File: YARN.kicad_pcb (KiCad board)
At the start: 2 copper layers, 99 x 91.7 mm, 12 parts, among them J1 Cart System Out, J2 Cart Main In, J3 Cart Sub In, SW1 SW_SPDT, U1 74HC244, U2 74HC244

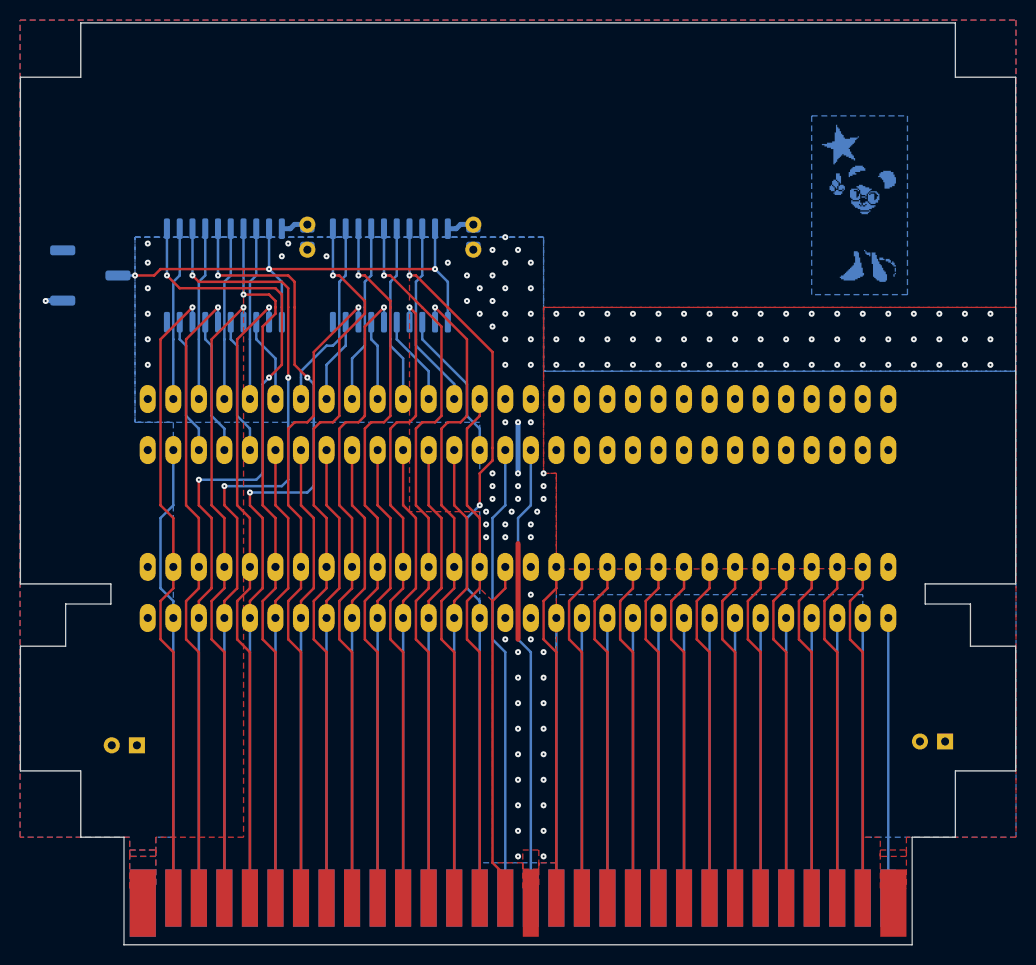
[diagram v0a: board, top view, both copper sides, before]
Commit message: Buffer data and addr bus, add switch for VRC6 A/B
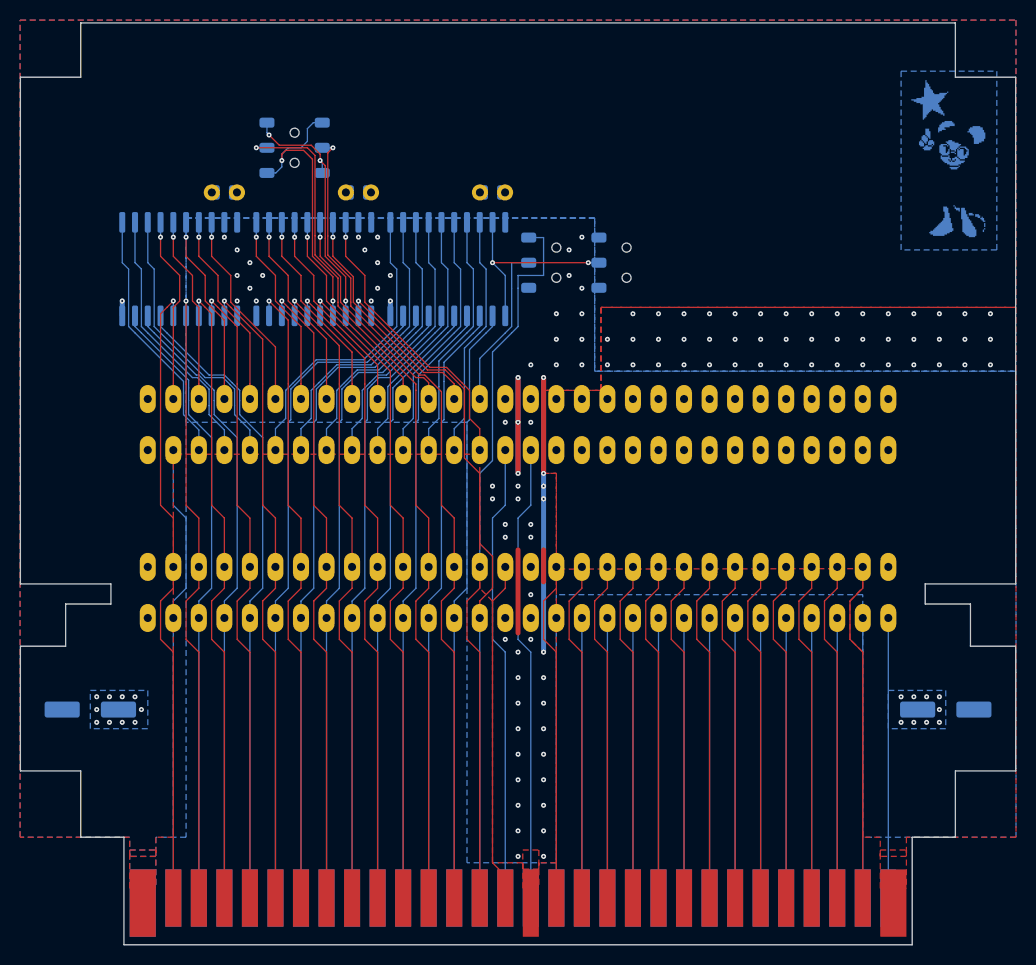
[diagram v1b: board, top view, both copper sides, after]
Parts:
- removed the C4 at (106.0, 67.3)
- added C2: 0.1uF, YARN:C_Disc-0805_D3.0mm_W1.6mm_P2.50mm, B.Cu at (111.1, 62.9)
- added C3: 0.1uF, YARN:C_Disc-0805_D3.0mm_W1.6mm_P2.50mm, B.Cu at (97.8, 62.9)
- added SW2: SW_SPDT, YARN:SK-3390A-L0, B.Cu at (130.8, 69.8)
- added SW3: SW_DPDT_x2, YARN:SS-3390S-L0, B.Cu at (104.8, 58.4)
- added U3: 74HC541, Package_SO:SOIC-20W_7.5x12.8mm_P1.27mm, B.Cu at (93.3, 70.5)
- C4: renamed from C2; footprint Capacitor_THT:CP_Radial_D5.0mm_P2.50mm -> Capacitor_SMD:CP_Elec_6.3x5.4
- C5: renamed from C3; footprint Capacitor_THT:CP_Radial_D5.0mm_P2.50mm -> Capacitor_SMD:CP_Elec_6.3x5.4
- J3: value Cart Sub In -> Cart Exp In
- LOGO-2: renamed from Ref**; value Val** -> YARN
- SW1: footprint YARN:JS102011SCQN -> YARN:SK-3390A-L0
- U1, U2: value 74HC244 -> 74HC541
- moved SW1 53.4 mm to (137.8, 69.8), turned to -90 degrees
- moved LOGO-2 11.4 mm to (149.9, 57.8)
- moved LOGO-1 9.94 mm to (169.5, 59.7)
- moved U2 8.91 mm to (106.7, 70.5)
- moved C5 5.84 mm to (84.5, 114.3), turned to 0 degrees
- moved U1 5.75 mm to (120.0, 70.5)
- moved C1 4.84 mm to (124.5, 62.9), turned to 180 degrees
- moved C4 3.18 mm to (169.5, 114.3), turned to 0 degrees
- renumbered REF** to LOGO-1
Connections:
- J3 pad 14: /CPU_R~{W} -> /S_CPU_R~{W}
- J3 pad 36: /CPU_D7 -> /S_CPU_D7
- J3 pad 37: /CPU_D6 -> /S_CPU_D6
- J3 pad 38: /CPU_D5 -> /S_CPU_D5
- J3 pad 39: /CPU_D4 -> /S_CPU_D4
- J3 pad 40: /CPU_D3 -> /S_CPU_D3
- J3 pad 41: /CPU_D2 -> /S_CPU_D2
- J3 pad 42: /CPU_D1 -> /S_CPU_D1
- J3 pad 43: /CPU_D0 -> /S_CPU_D0
- U1 pad 11: /CPU_A5 -> /S_CPU_D7
- U1 pad 12: /S_CPU_A6 -> /S_CPU_D6
- U1 pad 13: /CPU_A3 -> /S_CPU_D5
- U1 pad 14: /S_CPU_A4 -> /S_CPU_D4
- U1 pad 15: /CPU_A1 -> /S_CPU_D3
- U1 pad 16: /S_CPU_A2 -> /S_CPU_D2
- U1 pad 17: /~{ROMSEL} -> /S_CPU_D1
- U1 pad 18: /S_CPU_A0 -> /S_CPU_D0
- U1 pad 2: /CPU_A0 -> /CPU_D0
- U1 pad 3: /S_~{ROMSEL} -> /CPU_D1
- U1 pad 4: /CPU_A2 -> /CPU_D2
- U1 pad 5: /S_CPU_A1 -> /CPU_D3
- U1 pad 6: /CPU_A4 -> /CPU_D4
- U1 pad 7: /S_CPU_A3 -> /CPU_D5
- U1 pad 8: /CPU_A6 -> /CPU_D6
- U1 pad 9: /S_CPU_A5 -> /CPU_D7
- U2 pad 1: /S_~{CE} -> GND
- U2 pad 11: /CPU_A12 -> /S_CPU_A6
- U2 pad 12: /S_CPU_A11 -> /S_CPU_A5
- U2 pad 13: /CPU_A13 -> /S_CPU_A4
- U2 pad 14: /S_CPU_A10 -> /S_CPU_A3
- U2 pad 15: /CPU_A14 -> /S_CPU_A2
- U2 pad 16: /S_CPU_A9 -> /S_CPU_A1
- U2 pad 17: /CPU_A7 -> /S_CPU_A0
- U2 pad 18: /S_CPU_A8 -> /S_~{ROMSEL}
- U2 pad 19: /S_~{CE} -> GND
- U2 pad 2: /CPU_A8 -> /~{ROMSEL}
- U2 pad 3: /S_CPU_A7 -> /CPU_A0_V
- U2 pad 4: /CPU_A9 -> /CPU_A1_V
- U2 pad 5: /S_CPU_A14 -> /CPU_A2
- U2 pad 6: /CPU_A10 -> /CPU_A3
- U2 pad 7: /S_CPU_A13 -> /CPU_A4
- U2 pad 8: /CPU_A11 -> /CPU_A5
- U2 pad 9: /S_CPU_A12 -> /CPU_A6
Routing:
- net GND: track 16.3 -> 70.3 mm, vias 73 -> 76
- net /S_~{CE}: track 51.5 -> 20.4 mm, vias 3 -> 2
- net /S_CPU_D7: track 0.00 -> 30.7 mm
- net /CPU_A1_V: track 0.00 -> 29.7 mm, vias 0 -> 2
- net /S_CPU_D6: track 0.00 -> 29.4 mm
- net /S_CPU_D5: track 0.00 -> 28.1 mm
- net /S_CPU_D4: track 0.00 -> 26.9 mm
- net /S_CPU_D3: track 0.00 -> 25.8 mm
- net /CPU_A0_V: track 0.00 -> 25.6 mm, vias 0 -> 3
- net /S_CPU_D2: track 0.00 -> 25.3 mm
- net /S_CPU_D1: track 0.00 -> 24.8 mm
- net /S_CPU_D0: track 0.00 -> 24.2 mm
- net /CPU_A12: track 84.7 -> 61.6 mm, vias 3 -> 0
- net /CPU_R~{W}: track 51.7 -> 72.4 mm
- net /CPU_D7: track 45.6 -> 66.1 mm
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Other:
- board text added: "Dx PASS Dx Z"
- board text added: "R~{W} PASS ~{W}"
- board text added: "VRC6B VRC6A"

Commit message: Improve slide switch footprints
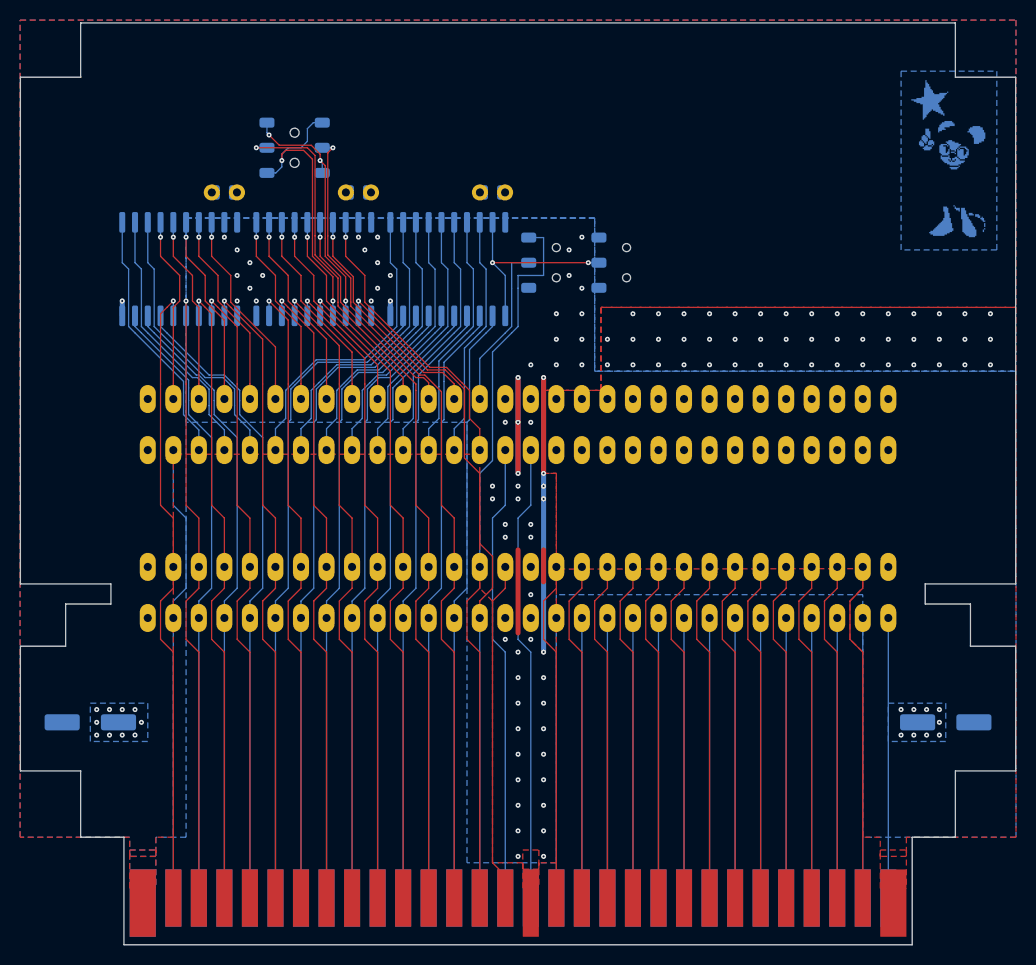
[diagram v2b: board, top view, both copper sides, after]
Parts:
- moved C4 1.27 mm to (169.5, 115.6)
- moved C5 1.27 mm to (84.5, 115.6)

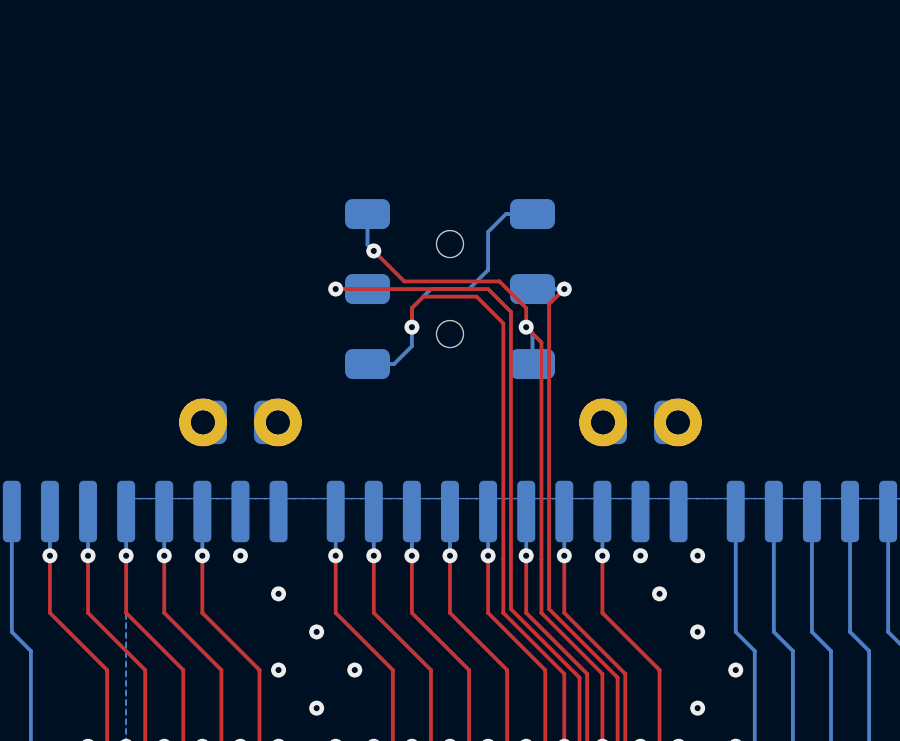
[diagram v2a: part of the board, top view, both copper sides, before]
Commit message: SS-3390S-L0 has slightly different dimensions
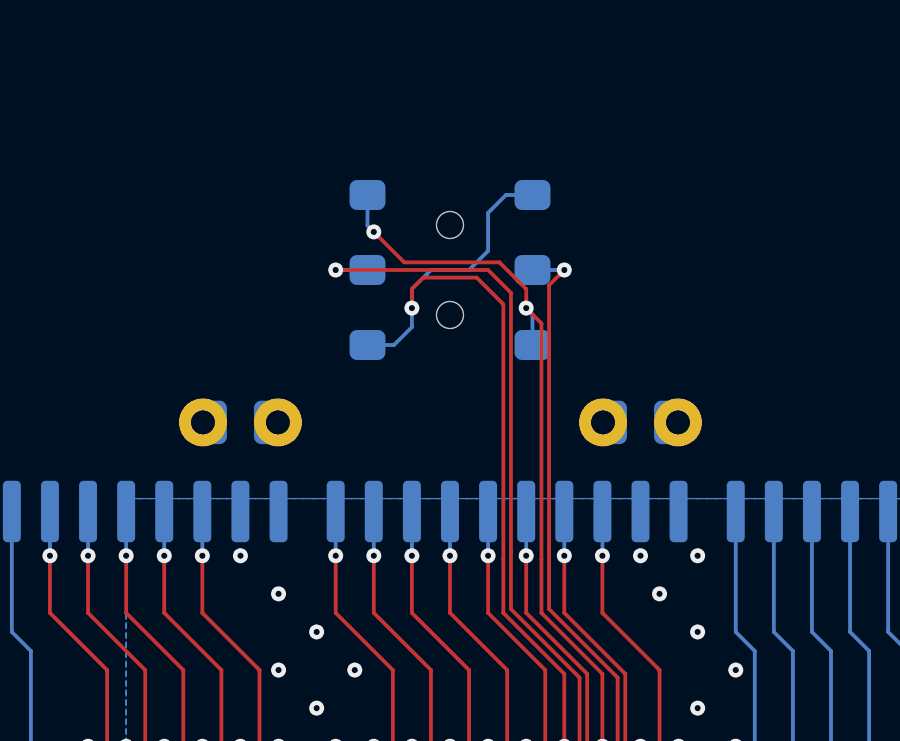
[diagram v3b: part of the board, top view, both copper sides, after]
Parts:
- moved SW3 0.64 mm to (104.8, 57.8)
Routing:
- net /CPU_A1: track 86.8 -> 87.5 mm
- net /CPU_A0_V: track 25.6 -> 26.3 mm
- net /CPU_A1_V: track 29.7 -> 30.3 mm
- net /CPU_A0: track 82.5 -> 83.1 mm

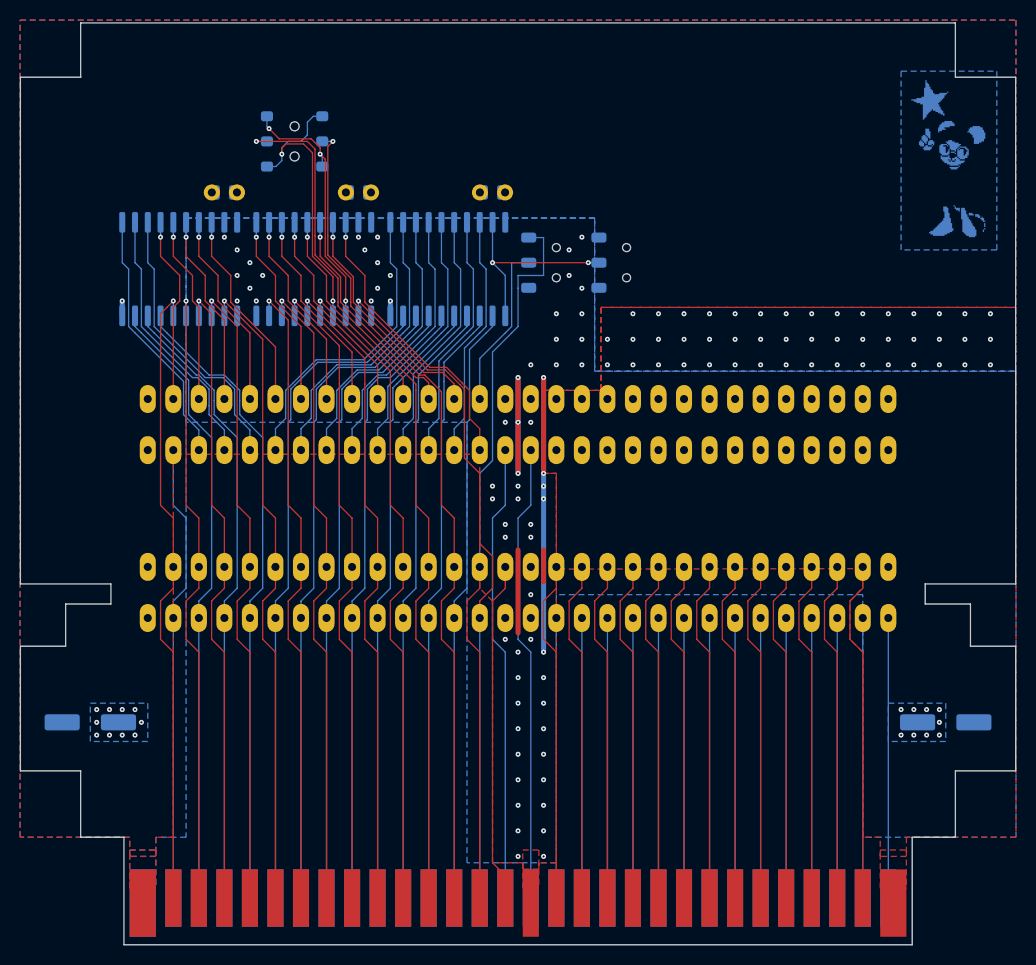
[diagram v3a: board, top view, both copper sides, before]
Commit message: Redesign decoding architecture
Thanks, lidnariq and Perkka!
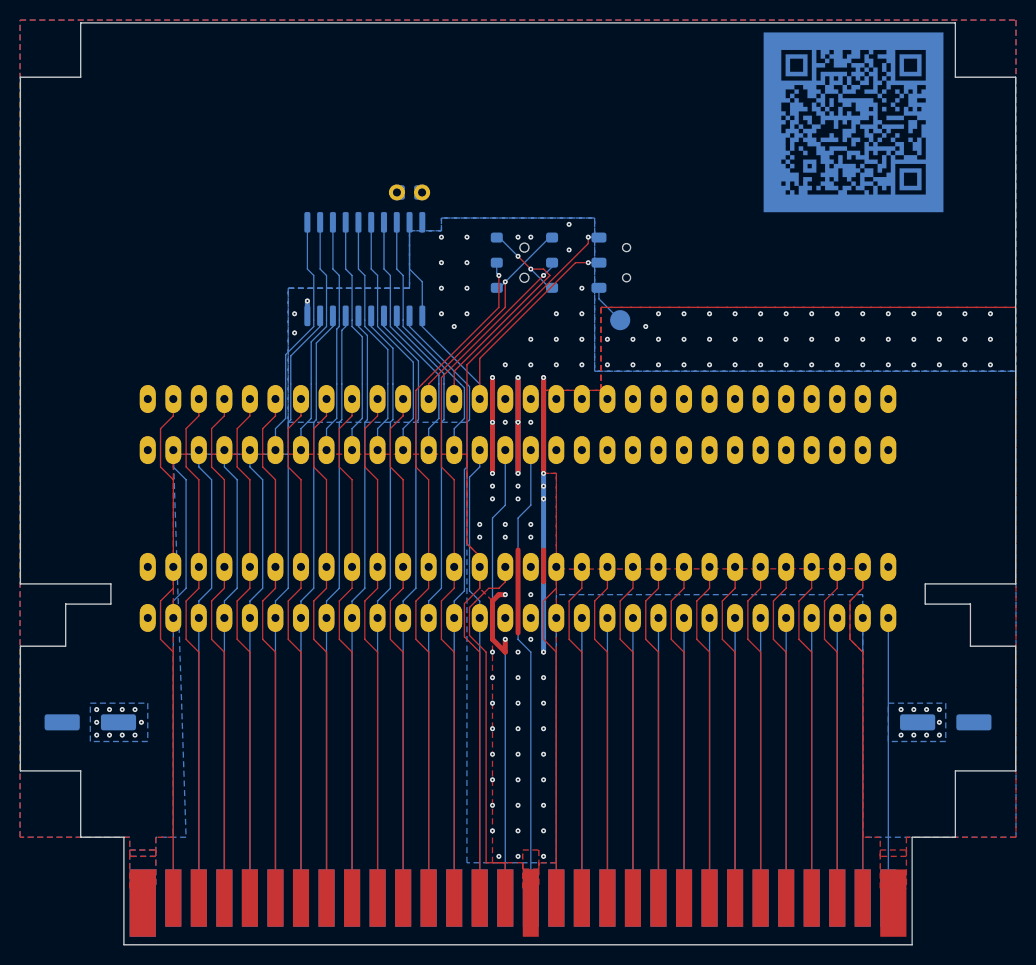
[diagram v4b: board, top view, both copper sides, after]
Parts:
- removed C2, C3: 0.1uF, YARN:C_Disc-0805_D3.0mm_W1.6mm_P2.50mm
- removed LOGO-1: dagga_star_yoeynsf, YARN:dagga_star_yoeynsf
- removed the SW2 at (130.8, 69.8)
- removed U2, U3: 74HC541, Package_SO:SOIC-20W_7.5x12.8mm_P1.27mm
- added TP1: EXP_~{CE}, TestPoint:TestPoint_Pad_D2.0mm, B.Cu at (137.2, 75.6)
- moved SW2 25.8 mm to (127.6, 69.8)
- moved C1 8.25 mm to (116.2, 62.9)
- moved U1 8.25 mm to (111.8, 70.5)
- moved LOGO-2 3.18 mm to (147.3, 55.9)
- renumbered SW3 to SW2
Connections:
- J3 pad 10: /S_CPU_A3 -> /CPU_A3
- J3 pad 11: /S_CPU_A2 -> /CPU_A2
- J3 pad 12: /S_CPU_A1 -> /CPU_A1_V
- J3 pad 13: /S_CPU_A0 -> /CPU_A0_V
- J3 pad 2: /S_CPU_A11 -> /CPU_A11
- J3 pad 3: /S_CPU_A10 -> /CPU_A10
- J3 pad 33: /S_CPU_A12 -> /CPU_A12
- J3 pad 34: /S_CPU_A13 -> /CPU_A13
- J3 pad 35: /S_CPU_A14 -> /CPU_A14
- J3 pad 4: /S_CPU_A9 -> /CPU_A9
- J3 pad 44: /S_~{ROMSEL} -> /~{ROMSEL}
- J3 pad 5: /S_CPU_A8 -> /CPU_A8
- J3 pad 56: VCC -> GND
- J3 pad 6: /S_CPU_A7 -> /CPU_A7
- J3 pad 7: /S_CPU_A6 -> /CPU_A6
- J3 pad 8: /S_CPU_A5 -> /CPU_A5
- J3 pad 9: /S_CPU_A4 -> /CPU_A4
- SW1 pad 1: GND -> /CPU_R~{W}
- SW1 pad 2: /S_~{CE} -> /S_CPU_R~{W}
- SW1 pad 3: VCC -> Net-(SW1-C)
- U1 pad 1: /S_~{CE} -> /S_CPU_R~{W}
- U1 pad 19: /S_~{CE} -> /S_CPU_R~{W}
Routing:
- net /S_~{ROMSEL}: track 29.1 -> 0.00 mm, vias 1 -> 0
- net /S_CPU_A14: track 27.9 -> 0.00 mm
- net /S_CPU_A13: track 26.6 -> 0.00 mm
- net GND: track 70.3 -> 96.2 mm, vias 76 -> 89
- net /S_CPU_A12: track 25.8 -> 0.00 mm
- net /S_CPU_R~{W}: track 16.6 -> 40.3 mm, vias 0 -> 1
- net /S_CPU_A0: track 23.7 -> 0.00 mm, vias 1 -> 0
- net /~{ROMSEL}: track 68.0 -> 45.4 mm, vias 1 -> 0
- net /S_CPU_A1: track 22.5 -> 0.00 mm, vias 1 -> 0
- net /S_CPU_A2: track 21.5 -> 0.00 mm, vias 1 -> 0
- net /S_CPU_A3: track 21.0 -> 0.00 mm, vias 1 -> 0
- net /S_CPU_A4: track 20.5 -> 0.00 mm, vias 1 -> 0
- net /S_~{CE}: track 20.4 -> 0.00 mm, vias 2 -> 0
- net /S_CPU_A7: track 20.2 -> 0.00 mm, vias 1 -> 0
- net /S_CPU_A5: track 19.9 -> 0.00 mm, vias 1 -> 0
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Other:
- board text added: "VRC6B NORMAL"
- board text added: "~{W} PASS TP PASS"
- board text removed: "Dx PASS Dx Z"
- board text removed: "R~{W} PASS ~{W}"
- board text removed: "VRC6B VRC6A"
